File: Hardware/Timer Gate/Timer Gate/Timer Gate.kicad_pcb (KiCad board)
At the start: 2 copper layers, 32 x 24.4 mm, 7 parts, among them J1 OUTPUT, J2 SENSOR, U1 Trinket

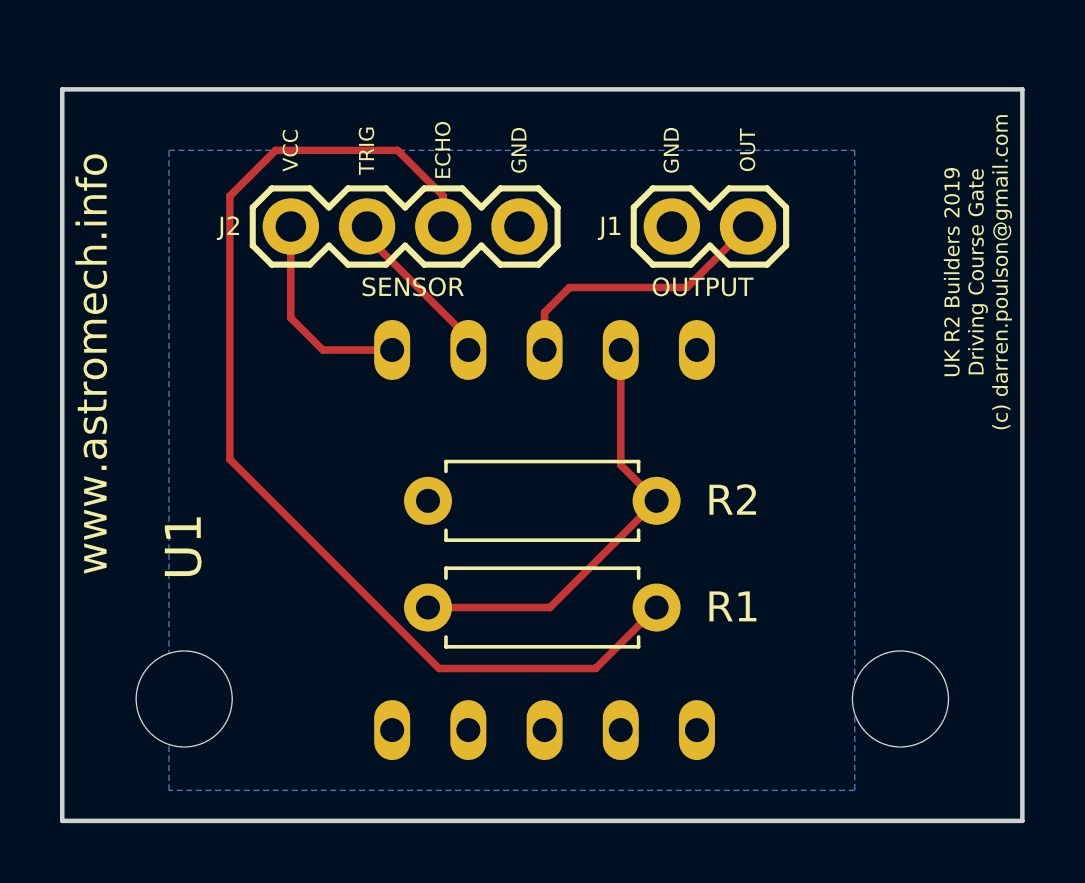
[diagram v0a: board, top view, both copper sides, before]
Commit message: Updated course gate PCB, and updated the strobe code
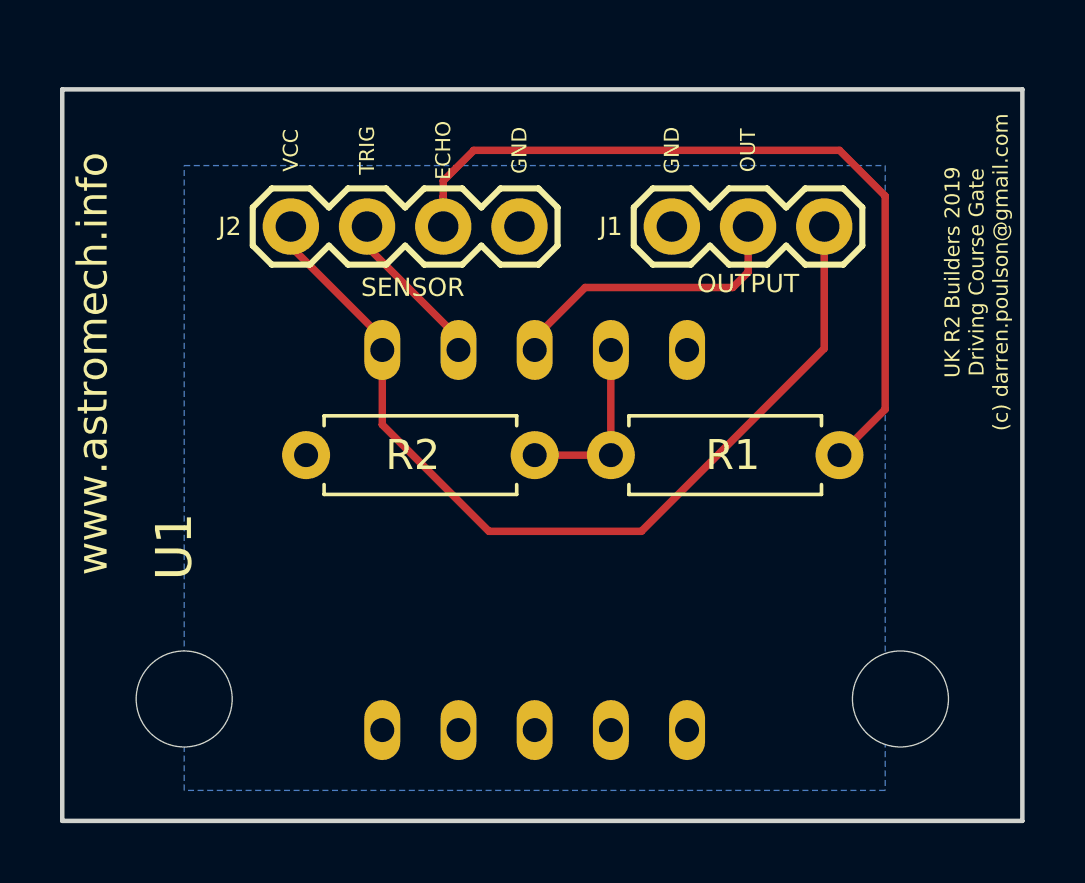
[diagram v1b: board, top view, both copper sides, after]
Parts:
- J1: footprint Connectors2:1X02 -> Connectors2:1X03
- moved R1 7.94 mm to (138.2, 86.9)
- moved R2 4.34 mm to (128.0, 86.9)
- moved U1 0.33 mm to (135.6, 89.7)
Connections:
- J2 pad 1: Net-(J2-Pad1) -> Net-(J1-Pad3)
- U1 pad 10: Net-(J2-Pad1) -> Net-(J1-Pad3)
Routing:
- net Net-(J1-Pad3): track 0.00 -> 30.7 mm
- net Net-(R1-Pad1): track 14.6 -> 6.04 mm
- net Net-(J2-Pad3): track 36.1 -> 27.6 mm
- net Net-(J2-Pad1): track 6.87 -> 0.00 mm
- net Net-(J1-Pad2): track 9.22 -> 9.94 mm
